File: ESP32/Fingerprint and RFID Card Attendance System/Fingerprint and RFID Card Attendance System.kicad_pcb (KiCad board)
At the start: 2 copper layers, 97.4 x 137.5 mm, 63 parts, among them J1 RTC, J11 V_OUT, J12 +BATT, J13 BUTTONS, J14 AS608, J15 SD MODULE, J16 -BATT, J17 SW_C, J18 SW_NO, J2 SCREEN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

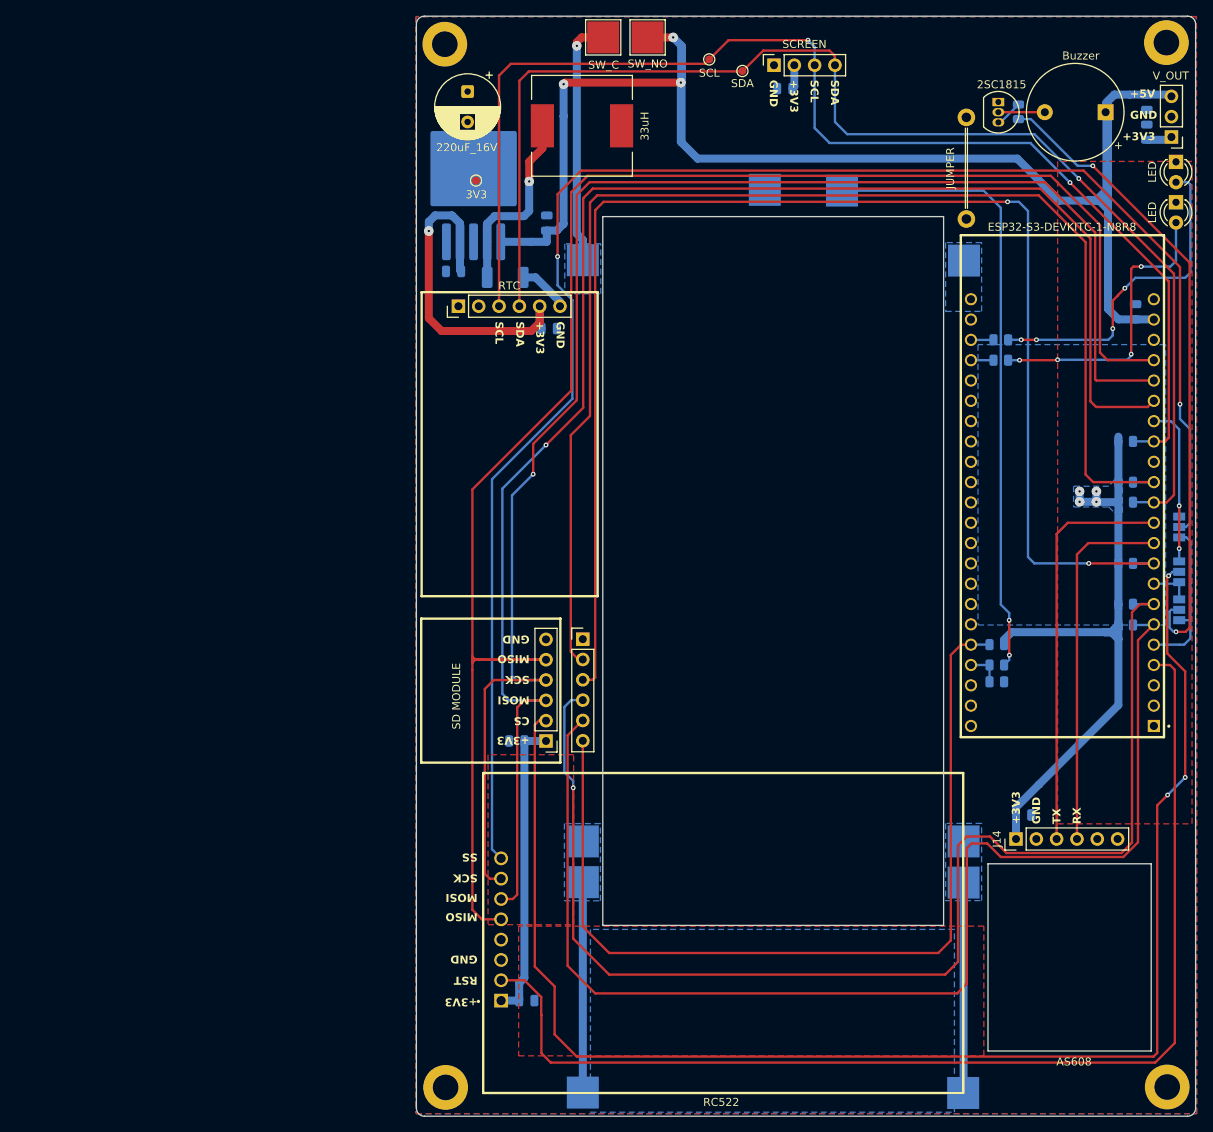
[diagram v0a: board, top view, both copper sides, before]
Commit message: Added more images
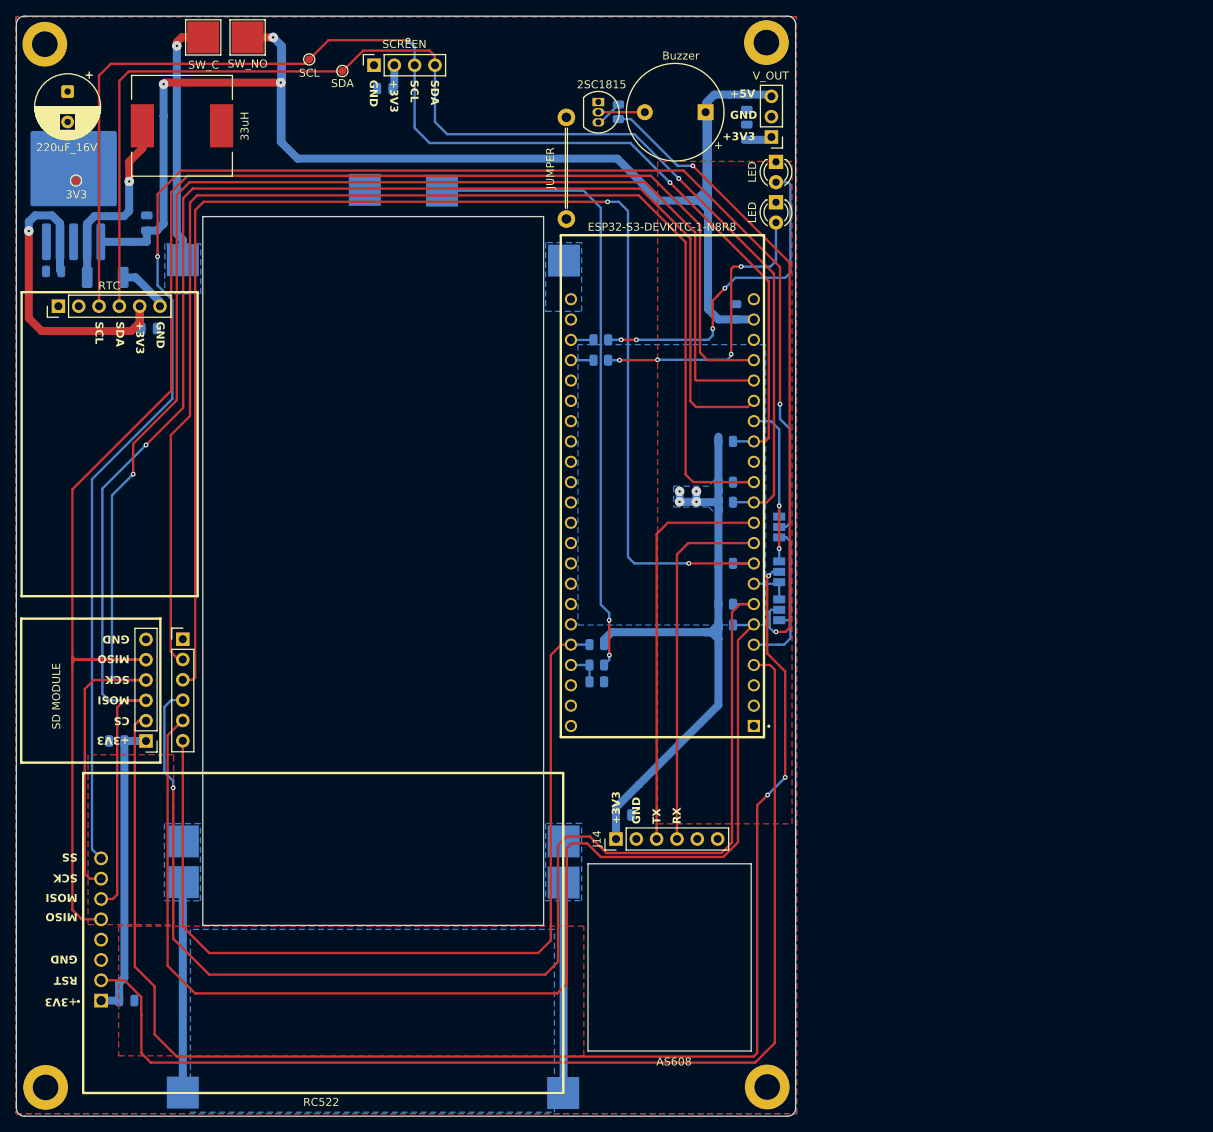
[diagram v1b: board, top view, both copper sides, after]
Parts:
- moved C1 50.0 mm to (90.0, 36.9)
- moved J16 50.0 mm to (87.5, 49.5)
- moved R11 50.0 mm to (116.5, 106.4)
- moved R3 50.0 mm to (117.0, 68.3)
- moved R4 50.0 mm to (117.0, 70.8)
- moved R5 50.0 mm to (116.5, 109.0)
- moved R6 50.0 mm to (116.5, 111.0)
- moved C8 50.0 mm to (48.6, 59.8)
- moved U2 50.0 mm to (51.1, 48.4)
- moved 3.3V5 50.0 mm to (51.5, 48.4)
- moved 5V1 50.0 mm to (77.1, 42.6)
- moved BZ1 50.0 mm to (130.2, 39.9)
- moved C10 50.0 mm to (119.9, 127.7)
- moved C11 50.0 mm to (56.5, 118.5)
- moved C3 50.0 mm to (133.9, 64.8)
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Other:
- outline, holes or cut-outs redrawn

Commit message: Updates from Work
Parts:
- moved R11 29.3 mm to (145.8, 106.4)
- moved R3 29.3 mm to (146.3, 68.3)
- moved R4 29.3 mm to (146.3, 70.8)
- moved R5 29.3 mm to (145.8, 109.0)
- moved R6 29.3 mm to (145.8, 111.0)
- moved C8 29.3 mm to (77.9, 59.8)
- moved U2 29.3 mm to (80.4, 48.4)
- moved 3.3V5 29.2 mm to (80.7, 48.4)
- moved 5V1 29.2 mm to (106.4, 42.6)
- moved BZ1 29.2 mm to (159.4, 39.9)
- moved C1 29.2 mm to (119.3, 36.9)
- moved C10 29.2 mm to (149.2, 127.7)
- moved C11 29.2 mm to (85.8, 118.5)
- moved C3 29.2 mm to (163.2, 64.8)
- moved C4 29.2 mm to (89.5, 53.7)
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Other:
- outline, holes or cut-outs redrawn
